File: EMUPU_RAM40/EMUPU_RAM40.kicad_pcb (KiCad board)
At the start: 2 copper layers, 99.1 x 73.7 mm, 26 parts, among them J1 Conn_01x20_Socket, J2 Conn_01x20_Socket, J3 Barrel_Jack_Switch, J4 Conn_01x06_Pin, J5 Conn_01x08_Pin, SW1 SW_SPDT, SW2 SW_SPST, U1 PIC18F47Q43-IP, U2 628128

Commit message: ram40 powerlines comleted, ready to start autoroute
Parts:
- moved JP1 166.7 mm to (97.1, 116.8)
- moved C2 161.2 mm to (97.8, 121.9), turned to 90 degrees
- moved SW2 140.8 mm to (122.4, 73.7)
- moved SW1 140.6 mm to (135.7, 67.3), turned to -90 degrees
- moved C1 130.4 mm to (137.2, 147.3), turned to 90 degrees
- moved D1 115.2 mm to (148.6, 82.5), turned to 90 degrees
- moved C3 113.2 mm to (115.6, 75.0), turned to -90 degrees
- moved R1 106.6 mm to (151.1, 74.9), turned to -90 degrees
- moved R2 104.3 mm to (153.6, 74.9), turned to -90 degrees
- moved R3 102.0 mm to (156.2, 74.9), turned to -90 degrees
- moved R5 99.0 mm to (158.8, 82.5), turned to 90 degrees
- moved D2 98.8 mm to (135.7, 77.5), turned to 90 degrees
- moved R6 96.8 mm to (161.3, 82.5), turned to 90 degrees
- moved C4 92.7 mm to (167.6, 127.0), turned to 180 degrees
- moved C5 89.9 mm to (167.6, 106.7), turned to 180 degrees
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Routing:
- net VCC: track 0.00 -> 298.6 mm, vias 0 -> 7
- net GND: track 0.00 -> 294.6 mm, vias 0 -> 8
- net Net-(SW1-C): track 0.00 -> 44.0 mm
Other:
- board size 99.1 x 73.7 mm -> 99.1 x 91.6 mm

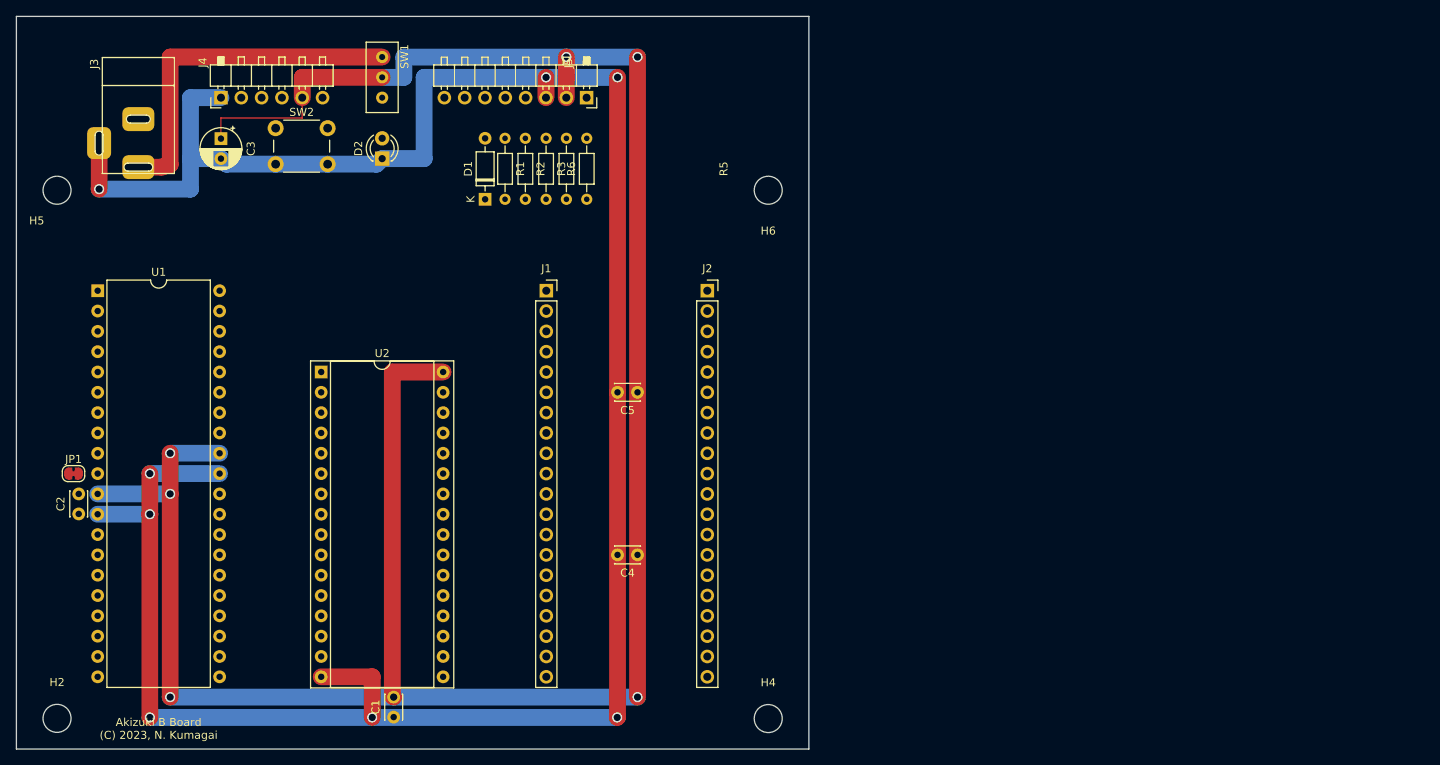
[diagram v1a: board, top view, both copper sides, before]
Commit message: before autorouting 2nd version, 48pin dummy socket included
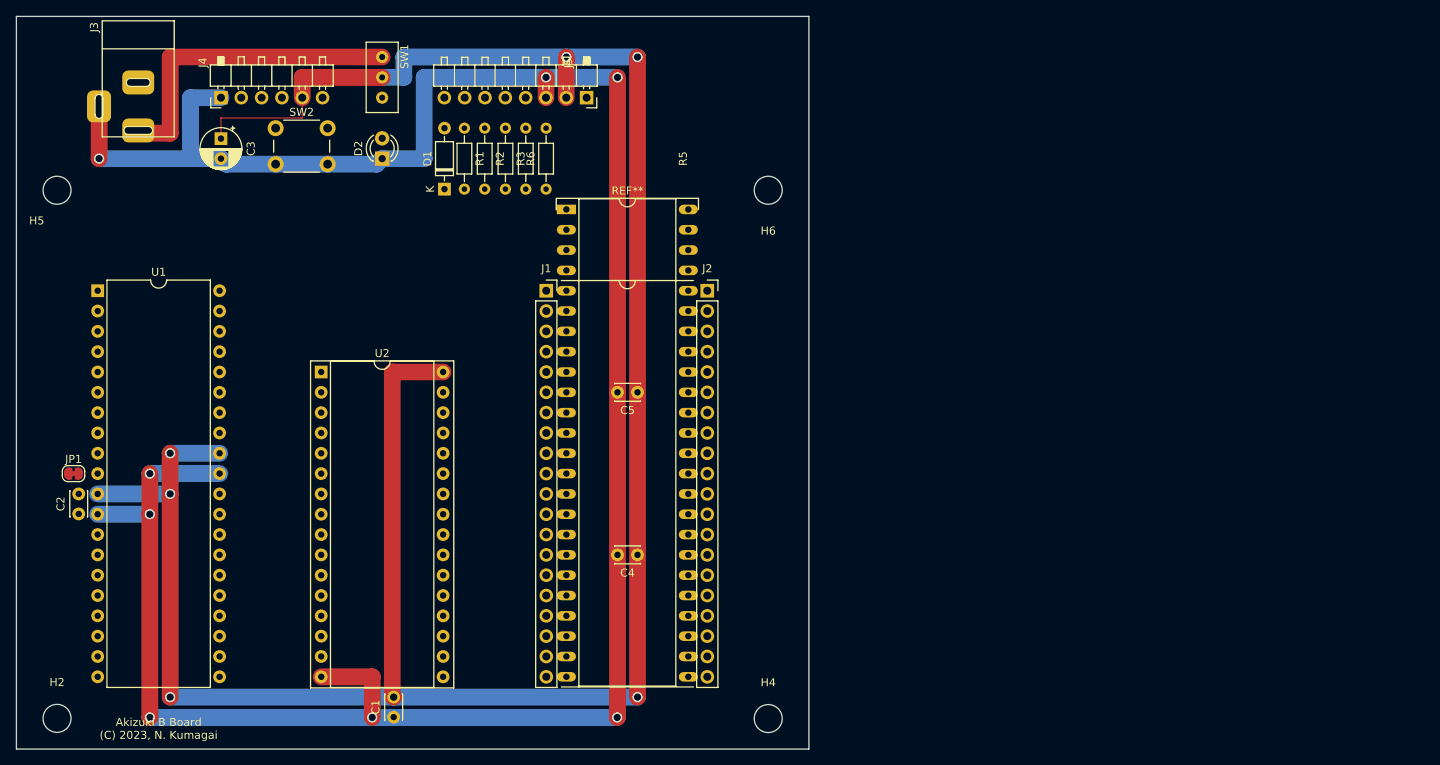
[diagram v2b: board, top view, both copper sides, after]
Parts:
- added REF**: DIP-48_W15.24mm_Socket_OvalPad_nocourtyard, 0-local:DIP-48_W15.24mm_Socket_OvalPad_splitcouryard, F.Cu at (158.8, 83.8)
- moved R1 5.24 mm to (146.0, 73.7)
- moved R2 5.24 mm to (148.5, 73.7)
- moved R3 5.24 mm to (151.1, 73.7)
- moved D1 5.24 mm to (143.5, 81.3)
- moved R5 5.24 mm to (153.7, 81.3)
- moved R6 5.24 mm to (156.2, 81.3)
- moved J3 4.59 mm to (105.2, 68.0)
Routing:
- net Net-(SW1-C): track 44.0 -> 40.0 mm
- net GND: track 294.6 -> 291.6 mm

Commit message: 3rd before-freerouting, add Z80 pin-names, beta-border, and narrower board size and rearrangement of parts
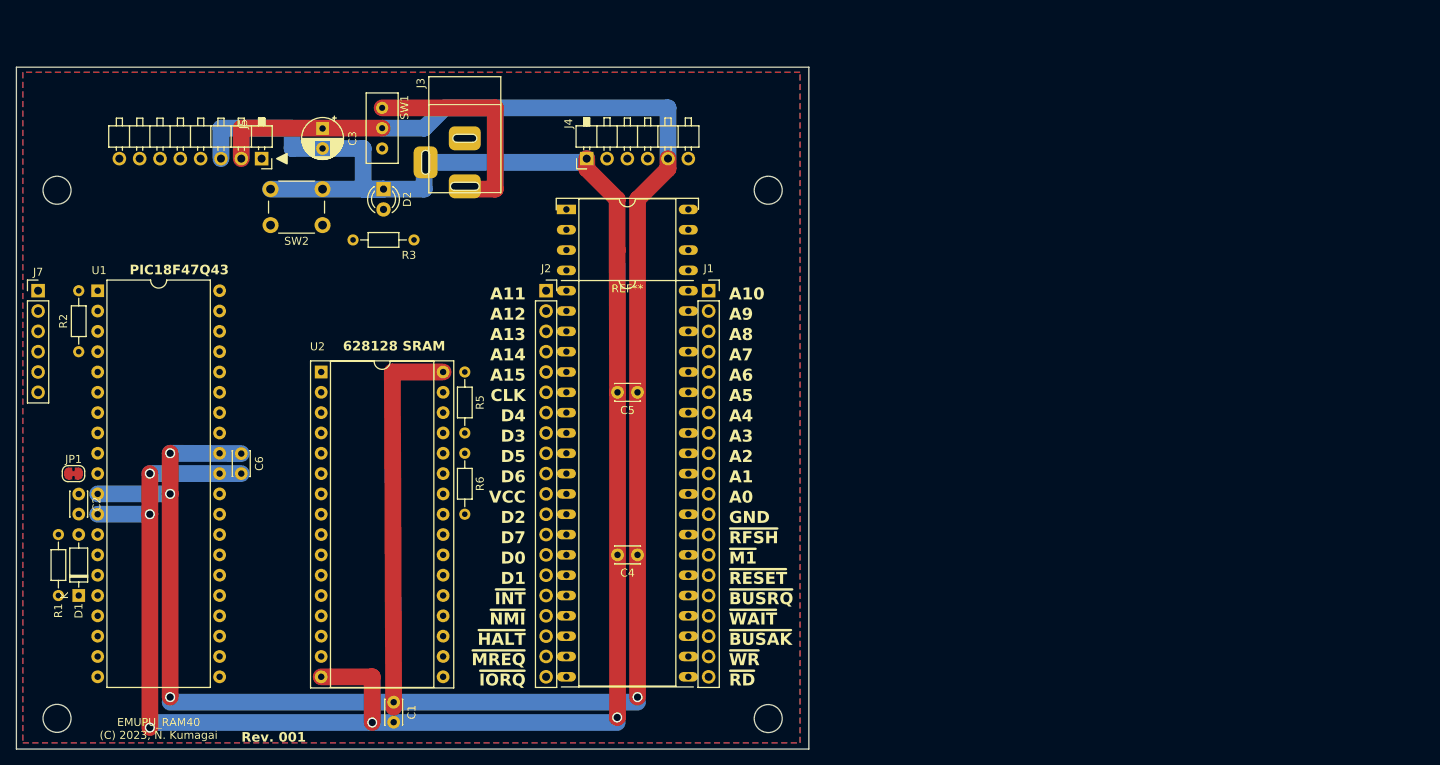
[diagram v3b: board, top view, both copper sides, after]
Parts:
- added C6: 0.1uF, Capacitor_THT:C_Disc_D3.0mm_W2.0mm_P2.50mm, F.Cu at (118.1, 114.3)
- added J7: PinHeader_1x06_P2.54mm_Vertical, Connector_PinHeader_2.54mm:PinHeader_1x06_P2.54mm_Vertical, F.Cu at (92.7, 94.0)
- moved R1 77.4 mm to (95.2, 132.1), turned to 90 degrees
- moved D1 68.3 mm to (97.8, 132.1)
- moved R2 57.9 mm to (97.8, 101.6), turned to 90 degrees
- moved J4 46.4 mm to (161.3, 77.5)
- moved J3 41.4 mm to (146.0, 74.9)
- moved J5 41.3 mm to (102.8, 77.5)
- moved R6 34.5 mm to (146.1, 114.3), turned to -90 degrees
- moved R5 31.4 mm to (146.1, 111.8)
- moved R3 23.6 mm to (132.1, 87.6), turned to 0 degrees
- moved J1 20.3 mm to (176.5, 94.0)
- moved J2 20.2 mm to (156.2, 94.0)
- moved SW2 13.5 mm to (128.3, 85.8), turned to 180 degrees
- moved C3 12.8 mm to (128.3, 73.7)
- moved SW1 6.35 mm to (135.7, 73.7)
- moved D2 3.81 mm to (135.9, 81.3), turned to -90 degrees
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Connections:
- J2 pad 16: VCC -> /~{INT}
- J2 pad 17: VCC -> /~{NMI}
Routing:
- net GND: track 291.6 -> 266.4 mm, vias 8 -> 5
- net Net-(SW1-C): track 40.0 -> 28.3 mm
- net VCC: track 298.6 -> 288.6 mm, vias 7 -> 4
- added copper zone on B.Cu, net GND
- added copper zone on F.Cu, net VCC
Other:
- board size 99.1 x 91.6 mm -> 99.1 x 85.2 mm
- board text added: "628128 SRAM"
- board text added: "A0"
- board text added: "A1"
- board text added: "A10"
- board text added: "A11"
- board text added: "A12"
- board text added: "A13"
- board text added: "A14"
- board text added: "A15"
- board text added: "A2"
- board text added: "A3"
- board text added: "A4"
- board text added: "A5"
- board text added: "A6"
- board text added: "A7"
- board text added: "A8"
- board text added: "A9"
- board text added: "CLK"
- board text added: "D0"
- board text added: "D1"
- board text added: "D2"
- board text added: "D3"
- board text added: "D4"
- board text added: "D5"
- board text added: "D6"
- board text added: "D7"
- board text added: "EMUPU_RAM40 (C) 2023, N. Kumagai"
- board text added: "GND"
- board text added: "PIC18F47Q43"
- board text added: "Rev. 001"
- board text added: "VCC"
- board text added: "~{BUSAK}"
- board text added: "~{BUSRQ}"
- board text added: "~{HALT}"
- board text added: "~{INT}"
- board text added: "~{IORQ}"
- board text added: "~{M1}"
- board text added: "~{MREQ}"
- board text added: "~{NMI}"
- board text added: "~{RD}"
- board text added: "~{RESET}"
- board text added: "~{RFSH}"
- board text added: "~{WAIT}"
- board text added: "~{WR}"
- board text removed: "Akizuki B Board (C) 2023, N. Kumagai"

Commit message: Loose some unconnected VCC/GND, move some Rs
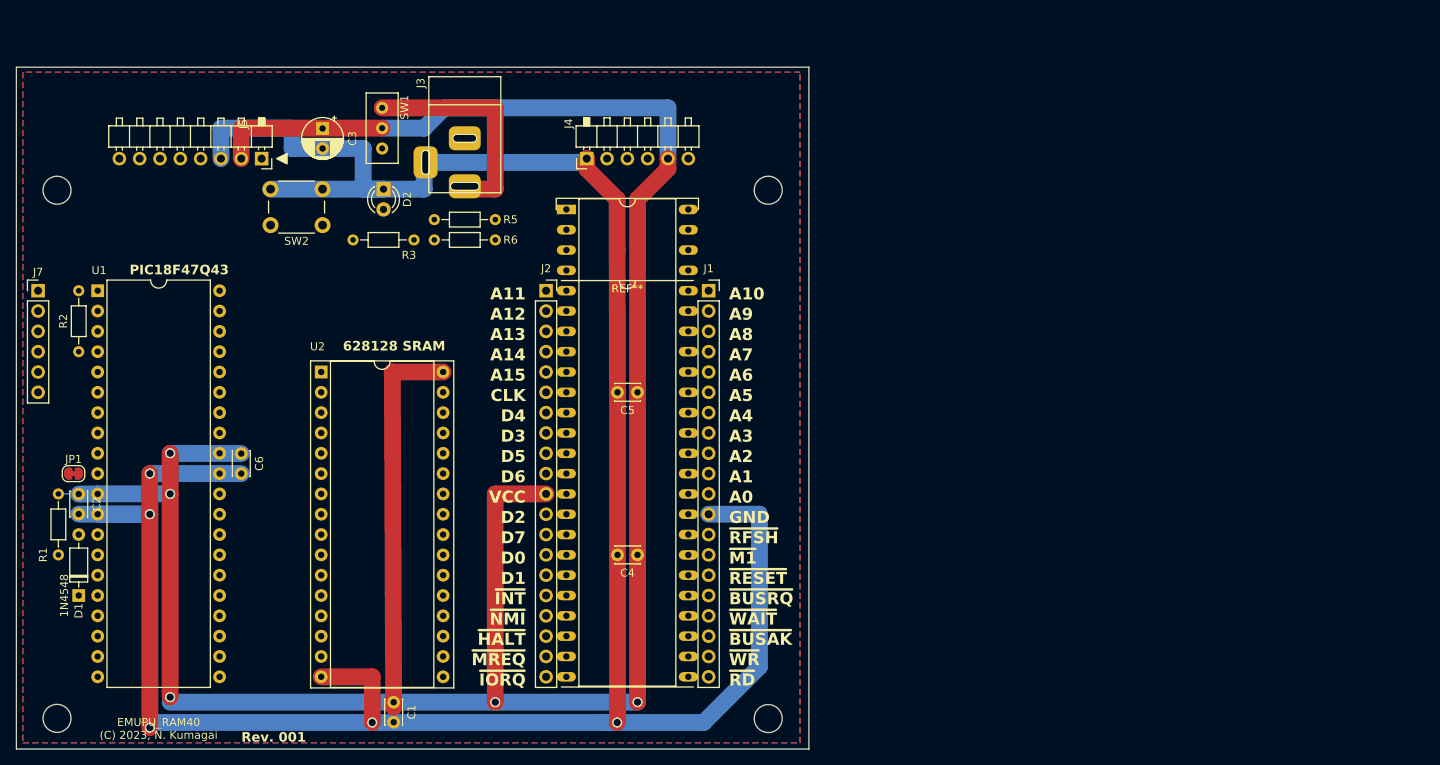
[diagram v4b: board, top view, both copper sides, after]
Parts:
- moved R5 26.9 mm to (149.9, 85.1), turned to 180 degrees
- moved R6 26.9 mm to (149.9, 87.6), turned to 180 degrees
- moved R1 12.7 mm to (95.2, 119.4), turned to -90 degrees
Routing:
- net GND: track 266.4 -> 323.9 mm
- net VCC: track 288.6 -> 326.5 mm, vias 4 -> 5
